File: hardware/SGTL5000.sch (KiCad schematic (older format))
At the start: 23 parts, among them J2 AudioJack3_Ground, J3 AudioJack3_Ground, U6 AP7313-1.8V, U7 SGTL5000

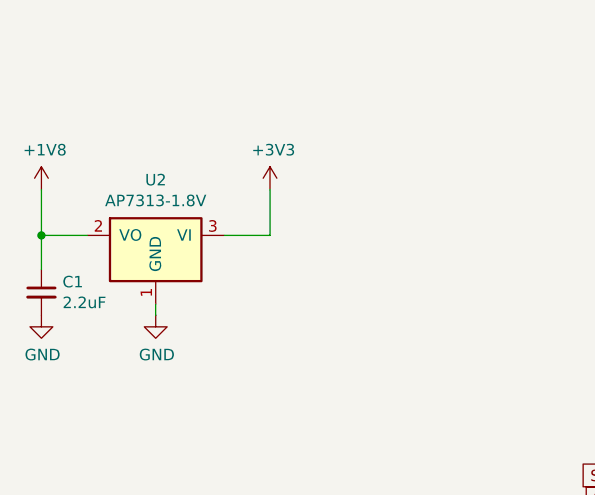
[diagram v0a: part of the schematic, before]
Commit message: notes, check current, add extra decoupling cap for reg, move led supply to 5v
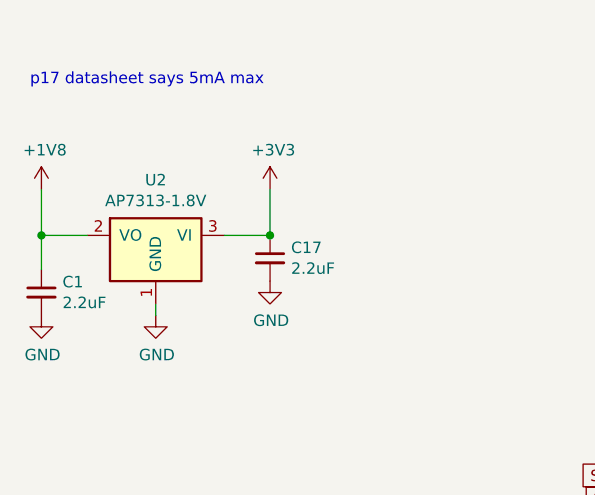
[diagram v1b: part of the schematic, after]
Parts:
- added C17: 2.2uF, Capacitor_SMD:C_0805_2012Metric, symbol Device:C_Small
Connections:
- net +3V3: now also C17.1
- net GND: now also C17.2
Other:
- note added: "p17 datasheet says 5mA max"
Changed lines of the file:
@@
 F 1 "AP7313-1.8V" H 2250 2251 50  0000 C CNN
 F 2 "Package_TO_SOT_SMD:SOT-23" H 2250 2100 50  0001 C CNN
-F 3 "" H 2250 2100 50  0001 C CNN
+F 3 "https://www.diodes.com/assets/Datasheets/AP7313.pdf" H 2250 2100 50  0001 C CNN
 	1    2250 2100
 	1    0    0    -1
@@
 Wire Wire Line
 	4350 3850 4950 3850
+Text Notes 1700 1450 0    50   ~ 0
+p17 datasheet says 5mA max
+$Comp
+L Device:C_Small C?
+U 1 1 5E1A3824
+P 2750 2200
+AR Path="/5E1A3824" Ref="C?"  Part="1"
+AR Path="/5BAC34FB/5E1A3824" Ref="C?"  Part="1"
+AR Path="/5E0E3867/5E1A3824" Ref="C17"  Part="1"
+F 0 "C17" H 2842 2246 50  0000 L CNN
+F 1 "2.2uF" H 2842 2155 50  0000 L CNN
+F 2 "Capacitor_SMD:C_0805_2012Metric" H 2750 2200 50  0001 C CNN
+F 3 "~" H 2750 2200 50  0001 C CNN
+	1    2750 2200
+	1    0    0    -1
+$EndComp
+Connection ~ 2750 2100
+$Comp
+L power:GND #PWR?
+U 1 1 5E1A3C62
+P 2750 2300
+AR Path="/5E1A3C62" Ref="#PWR?"  Part="1"
+AR Path="/5BAC34FB/5E1A3C62" Ref="#PWR?"  Part="1"
+AR Path="/5E0E3867/5E1A3C62" Ref="#PWR03"  Part="1"
+F 0 "#PWR03" H 2750 2050 50  0001 C CNN
+F 1 "GND" H 2755 2127 50  0000 C CNN
+F 2 "" H 2750 2300 50  0001 C CNN
+F 3 "" H 2750 2300 50  0001 C CNN
+	1    2750 2300
+	1    0    0    -1
+$EndComp
 $EndSCHEMATC

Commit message: footprints
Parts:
- C14, C15, C8, C9: value 2.2uF -> 1uF; footprint Capacitor_SMD:C_0805_2012Metric -> Capacitor_SMD:C_1210_3225Metric; farnell (none) -> 2112915
- J2, J3: footprint Connector_Audio:Jack_3.5mm_CUI_SJ-3523-SMT_Horizontal -> audio-fx:Jack_3.5mm_CUI_SJ-3523-SMT_Horizontal; farnell (none) -> 2915138
- U7: farnell (none) -> 2308049
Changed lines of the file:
@@
 F 0 "J1" H 7600 3000 50  0000 R CNN
 F 1 "AudioJack3_Ground" H 7500 3100 50  0001 R CNN
-F 2 "Connector_Audio:Jack_3.5mm_CUI_SJ-3523-SMT_Horizontal" H 7900 3050 50  0001 C CNN
+F 2 "audio-fx:Jack_3.5mm_CUI_SJ-3523-SMT_Horizontal" H 7900 3050 50  0001 C CNN
 F 3 "https://uk.farnell.com/switchcraft-conxall/35rasmt2bhntrx/connector-smt-3-5mm-ph-jk-tap/dp/2915138" H 7900 3050 50  0001 C CNN
+F 4 "2915138" H 7900 3050 50  0001 C CNN "farnell"
 	1    7900 3050
 	-1   0    0    1
@@
 F 0 "J2" H 7600 4150 50  0000 R CNN
 F 1 "AudioJack3_Ground" H 7550 4050 50  0001 R CNN
-F 2 "Connector_Audio:Jack_3.5mm_CUI_SJ-3523-SMT_Horizontal" H 7900 4200 50  0001 C CNN
+F 2 "audio-fx:Jack_3.5mm_CUI_SJ-3523-SMT_Horizontal" H 7900 4200 50  0001 C CNN
 F 3 "~" H 7900 4200 50  0001 C CNN
+F 4 "2915138" H 7900 4200 50  0001 C CNN "farnell"
 	1    7900 4200
 	-1   0    0    1
@@
 AR Path="/5BAC34FB/5BAC3E38" Ref="U7"  Part="1"
 AR Path="/5E0E3867/5BAC3E38" Ref="U3"  Part="1"
-F 0 "U3" H 5650 5000 60  0000 C CNN
-F 1 "SGTL5000" H 5650 4894 60  0000 C CNN
+F 0 "U3" H 5650 3750 60  0000 C CNN
+F 1 "SGTL5000" H 5600 2200 60  0000 C CNN
 F 2 "Package_DFN_QFN:QFN-32-1EP_5x5mm_P0.5mm_EP3.6x3.6mm" H 5650 3800 60  0001 C CNN
 F 3 "https://www.nxp.com/docs/en/data-sheet/SGTL5000.pdf" H 5600 2100 60  0000 C CNN
+F 4 "2308049" H 5650 3750 50  0001 C CNN "farnell"
 	1    5650 3750
 	1    0    0    -1
@@
 AR Path="/5E0E3867/5E146D40" Ref="C8"  Part="1"
 F 0 "C8" V 7042 2996 50  0000 L CNN
-F 1 "2.2uF" V 7150 2900 50  0000 L CNN
-F 2 "Capacitor_SMD:C_0805_2012Metric" H 6950 2950 50  0001 C CNN
-F 3 "~" H 6950 2950 50  0001 C CNN
+F 1 "1uF" V 7150 2900 50  0000 L CNN
+F 2 "Capacitor_SMD:C_1210_3225Metric" H 6950 2950 50  0001 C CNN
+F 3 "http://www.farnell.com/datasheets/199119.pdf" H 6950 2950 50  0001 C CNN
+F 4 "2112915" V 6950 2950 50  0001 C CNN "farnell"
 	1    6950 2950
 	0    -1   -1   0
@@
 AR Path="/5E0E3867/5E147768" Ref="C9"  Part="1"
 F 0 "C9" V 7050 3300 50  0000 L CNN
-F 1 "2.2uF" V 7150 3200 50  0000 L CNN
-F 2 "Capacitor_SMD:C_0805_2012Metric" H 6950 3250 50  0001 C CNN
+F 1 "1uF" V 7150 3200 50  0000 L CNN
+F 2 "Capacitor_SMD:C_1210_3225Metric" H 6950 3250 50  0001 C CNN
 F 3 "~" H 6950 3250 50  0001 C CNN
+F 4 "2112915" H 6950 3250 50  0001 C CNN "farnell"
 	1    6950 3250
 	0    -1   -1   0
@@
 F 0 "J3" H 7600 3750 50  0000 R CNN
 F 1 "AudioJack3_Ground" H 7550 3650 50  0001 R CNN
-F 2 "Connector_Audio:Jack_3.5mm_CUI_SJ-3523-SMT_Horizontal" H 7900 3800 50  0001 C CNN
+F 2 "audio-fx:Jack_3.5mm_CUI_SJ-3523-SMT_Horizontal" H 7900 3800 50  0001 C CNN
 F 3 "~" H 7900 3800 50  0001 C CNN
+F 4 "2915138" H 7900 3800 50  0001 C CNN "farnell"
 	1    7900 3800
 	-1   0    0    1
@@
 AR Path="/5E0E3867/5E1434E0" Ref="C14"  Part="1"
 F 0 "C14" V 7050 3350 50  0000 L CNN
-F 1 "2.2uF" V 7150 3300 50  0000 L CNN
-F 2 "Capacitor_SMD:C_0805_2012Metric" H 6950 3550 50  0001 C CNN
+F 1 "1uF" V 7150 3300 50  0000 L CNN
+F 2 "Capacitor_SMD:C_1210_3225Metric" H 6950 3550 50  0001 C CNN
 F 3 "~" H 6950 3550 50  0001 C CNN
+F 4 "2112915" H 6950 3550 50  0001 C CNN "farnell"
 	1    6950 3550
 	0    -1   -1   0
@@
 AR Path="/5E0E3867/5E143FCC" Ref="C15"  Part="1"
 F 0 "C15" V 6650 3750 50  0000 L CNN
-F 1 "2.2uF" V 6750 3650 50  0000 L CNN
-F 2 "Capacitor_SMD:C_0805_2012Metric" H 6950 3750 50  0001 C CNN
+F 1 "1uF" V 6750 3650 50  0000 L CNN
+F 2 "Capacitor_SMD:C_1210_3225Metric" H 6950 3750 50  0001 C CNN
 F 3 "~" H 6950 3750 50  0001 C CNN
+F 4 "2112915" H 6950 3750 50  0001 C CNN "farnell"
 	1    6950 3750
 	0    -1   -1   0

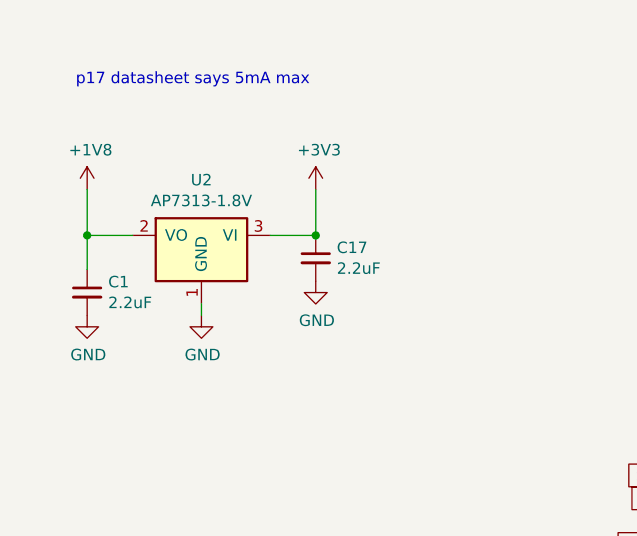
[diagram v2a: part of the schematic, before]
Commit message: changed to LDO that I can source from farnell
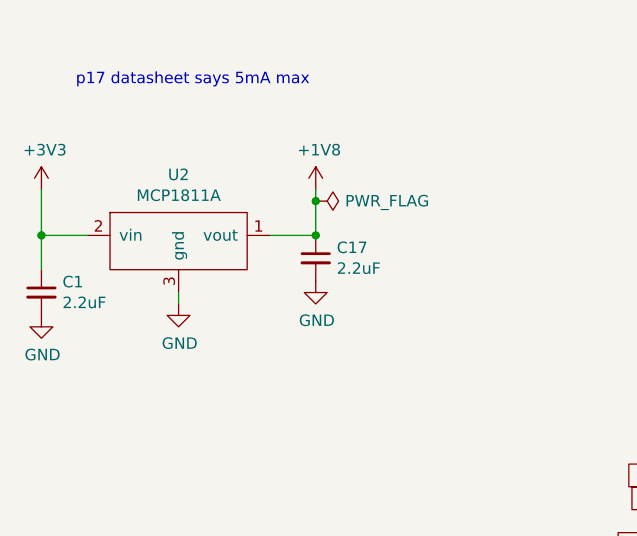
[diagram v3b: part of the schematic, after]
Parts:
- removed U6: AP7313-1.8V, Package_TO_SOT_SMD:SOT-23, symbol teensy-fx-rescue:teensy_beats_parts_AP7313R-1.8V-teensy_beats-cache
- added U2: MCP1811A, Package_TO_SOT_SMD:SOT-23, symbol teensy-fx-rescue:ldo
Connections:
- net +1V8: now also C17.1, U2.1 (vout); no longer C31.1
- net +3V3: now also C31.1, U2.2 (vin); no longer C17.1
- net GND: now also U2.3 (gnd)
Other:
- moved on the sheet: C1
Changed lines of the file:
@@
 	6050 2000 6350 2000
 Connection ~ 6050 2000
-$Comp
-L teensy-fx-rescue:teensy_beats_parts_AP7313R-1.8V-teensy_beats-cache U?
-U 1 1 5BAC54DA
-P 2250 2100
-AR Path="/5BAC54DA" Ref="U?"  Part="1"
-AR Path="/5BAC34FB/5BAC54DA" Ref="U6"  Part="1"
-AR Path="/5E0E3867/5BAC54DA" Ref="U2"  Part="1"
-F 0 "U2" H 2250 2342 50  0000 C CNN
-F 1 "AP7313-1.8V" H 2250 2251 50  0000 C CNN
-F 2 "Package_TO_SOT_SMD:SOT-23" H 2250 2100 50  0001 C CNN
-F 3 "https://www.diodes.com/assets/Datasheets/AP7313.pdf" H 2250 2100 50  0001 C CNN
-	1    2250 2100
-	1    0    0    -1
-$EndComp
-$Comp
-L Device:C_Small C?
-U 1 1 5BAC54E1
-P 1750 2350
-AR Path="/5BAC54E1" Ref="C?"  Part="1"
-AR Path="/5BAC34FB/5BAC54E1" Ref="C31"  Part="1"
-AR Path="/5E0E3867/5BAC54E1" Ref="C1"  Part="1"
-F 0 "C1" H 1842 2396 50  0000 L CNN
-F 1 "2.2uF" H 1842 2305 50  0000 L CNN
-F 2 "Capacitor_SMD:C_0805_2012Metric" H 1750 2350 50  0001 C CNN
-F 3 "~" H 1750 2350 50  0001 C CNN
-	1    1750 2350
-	1    0    0    -1
-$EndComp
-$Comp
-L power:GND #PWR?
-U 1 1 5BAC54E8
-P 1750 2450
-AR Path="/5BAC54E8" Ref="#PWR?"  Part="1"
-AR Path="/5BAC34FB/5BAC54E8" Ref="#PWR0133"  Part="1"
-AR Path="/5E0E3867/5BAC54E8" Ref="#PWR0116"  Part="1"
-F 0 "#PWR0116" H 1750 2200 50  0001 C CNN
-F 1 "GND" H 1755 2277 50  0000 C CNN
-F 2 "" H 1750 2450 50  0001 C CNN
-F 3 "" H 1750 2450 50  0001 C CNN
-	1    1750 2450
-	1    0    0    -1
-$EndComp
-Wire Wire Line
-	1950 2100 1750 2100
-Wire Wire Line
-	1750 2100 1750 2250
-Wire Wire Line
-	2250 2450 2250 2400
+Wire Wire Line
+	2150 2400 2150 2350
 Wire Wire Line
 	2550 2100 2750 2100
 Wire Wire Line
-	2750 2100 2750 1900
-Wire Wire Line
-	1750 2100 1750 1900
-Connection ~ 1750 2100
+	2750 2100 2750 1950
 $Comp
 L power:+3V3 #PWR?
 U 1 1 5BAC54FB
-P 2750 1900
+P 1550 1900
 AR Path="/5BAC54FB" Ref="#PWR?"  Part="1"
 AR Path="/5BAC34FB/5BAC54FB" Ref="#PWR0124"  Part="1"
 AR Path="/5E0E3867/5BAC54FB" Ref="#PWR0118"  Part="1"
-F 0 "#PWR0118" H 2750 1750 50  0001 C CNN
-F 1 "+3V3" H 2765 2073 50  0000 C CNN
-F 2 "" H 2750 1900 50  0001 C CNN
-F 3 "" H 2750 1900 50  0001 C CNN
-	1    2750 1900
-	1    0    0    -1
-$EndComp
-$Comp
-L power:+1V8 #PWR?
-U 1 1 5BAC5501
-P 1750 1900
-AR Path="/5BAC5501" Ref="#PWR?"  Part="1"
-AR Path="/5BAC34FB/5BAC5501" Ref="#PWR0123"  Part="1"
-AR Path="/5E0E3867/5BAC5501" Ref="#PWR0119"  Part="1"
-F 0 "#PWR0119" H 1750 1750 50  0001 C CNN
-F 1 "+1V8" H 1765 2073 50  0000 C CNN
-F 2 "" H 1750 1900 50  0001 C CNN
-F 3 "" H 1750 1900 50  0001 C CNN
-	1    1750 1900
+F 0 "#PWR0118" H 1550 1750 50  0001 C CNN
+F 1 "+3V3" H 1565 2073 50  0000 C CNN
+F 2 "" H 1550 1900 50  0001 C CNN
+F 3 "" H 1550 1900 50  0001 C CNN
+	1    1550 1900
 	1    0    0    -1
 $EndComp
@@
 L power:GND #PWR?
 U 1 1 5BAC54EE
-P 2250 2450
+P 2150 2400
 AR Path="/5BAC54EE" Ref="#PWR?"  Part="1"
 AR Path="/5BAC34FB/5BAC54EE" Ref="#PWR0134"  Part="1"
 AR Path="/5E0E3867/5BAC54EE" Ref="#PWR0117"  Part="1"
-F 0 "#PWR0117" H 2250 2200 50  0001 C CNN
-F 1 "GND" H 2255 2277 50  0000 C CNN
-F 2 "" H 2250 2450 50  0001 C CNN
-F 3 "" H 2250 2450 50  0001 C CNN
-	1    2250 2450
+F 0 "#PWR0117" H 2150 2150 50  0001 C CNN
+F 1 "GND" H 2155 2227 50  0000 C CNN
+F 2 "" H 2150 2400 50  0001 C CNN
+F 3 "" H 2150 2400 50  0001 C CNN
+	1    2150 2400
 	1    0    0    -1
 $EndComp
@@
 	1    0    0    -1
 $EndComp
+$Comp
+L teensy-fx-rescue:ldo U2
+U 1 1 5E1AE9E1
+P 2150 2100
+F 0 "U2" H 2150 2365 50  0000 C CNN
+F 1 "MCP1811A" H 2150 2274 50  0000 C CNN
+F 2 "Package_TO_SOT_SMD:SOT-23" H 2150 2100 50  0001 C CNN
+F 3 "http://www.farnell.com/datasheets/2722379.pdf" H 2150 2100 50  0001 C CNN
+F 4 "2990195" H 2150 2100 50  0001 C CNN "farnell"
+	1    2150 2100
+	1    0    0    -1
+$EndComp
+$Comp
+L power:+1V8 #PWR?
+U 1 1 5BAC5501
+P 2750 1900
+AR Path="/5BAC5501" Ref="#PWR?"  Part="1"
+AR Path="/5BAC34FB/5BAC5501" Ref="#PWR0123"  Part="1"
+AR Path="/5E0E3867/5BAC5501" Ref="#PWR0119"  Part="1"
+F 0 "#PWR0119" H 2750 1750 50  0001 C CNN
+F 1 "+1V8" H 2765 2073 50  0000 C CNN
+F 2 "" H 2750 1900 50  0001 C CNN
+F 3 "" H 2750 1900 50  0001 C CNN
+	1    2750 1900
+	1    0    0    -1
+$EndComp
+Connection ~ 1550 2100
+Wire Wire Line
+	1550 2100 1550 1900
+Wire Wire Line
+	1550 2100 1550 2250
+Wire Wire Line
+	1750 2100 1550 2100
+$Comp
+L power:GND #PWR?
+U 1 1 5BAC54E8
+P 1550 2450
+AR Path="/5BAC54E8" Ref="#PWR?"  Part="1"
+AR Path="/5BAC34FB/5BAC54E8" Ref="#PWR0133"  Part="1"
+AR Path="/5E0E3867/5BAC54E8" Ref="#PWR0116"  Part="1"
+F 0 "#PWR0116" H 1550 2200 50  0001 C CNN
+F 1 "GND" H 1555 2277 50  0000 C CNN
+F 2 "" H 1550 2450 50  0001 C CNN
+F 3 "" H 1550 2450 50  0001 C CNN
+	1    1550 2450
+	1    0    0    -1
+$EndComp
+$Comp
+L Device:C_Small C?
+U 1 1 5BAC54E1
+P 1550 2350
+AR Path="/5BAC54E1" Ref="C?"  Part="1"
+AR Path="/5BAC34FB/5BAC54E1" Ref="C31"  Part="1"
+AR Path="/5E0E3867/5BAC54E1" Ref="C1"  Part="1"
+F 0 "C1" H 1642 2396 50  0000 L CNN
+F 1 "2.2uF" H 1642 2305 50  0000 L CNN
+F 2 "Capacitor_SMD:C_0805_2012Metric" H 1550 2350 50  0001 C CNN
+F 3 "~" H 1550 2350 50  0001 C CNN
+	1    1550 2350
+	1    0    0    -1
+$EndComp
+$Comp
+L power:PWR_FLAG #FLG0104
+U 1 1 5E1CE9B1
+P 2750 1950
+F 0 "#FLG0104" H 2750 2025 50  0001 C CNN
+F 1 "PWR_FLAG" V 2750 2078 50  0000 L CNN
+F 2 "" H 2750 1950 50  0001 C CNN
+F 3 "~" H 2750 1950 50  0001 C CNN
+	1    2750 1950
+	0    1    1    0
+$EndComp
+Connection ~ 2750 1950
+Wire Wire Line
+	2750 1950 2750 1900
 $EndSCHEMATC

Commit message: farnell numbers
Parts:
- C13, C2, C27, C28, C30: farnell (none) -> 1414663
- C17, C26, C29, C31: farnell (none) -> 2773238
- L2: farnell (none) -> 2215655
- R22, R23: farnell (none) -> 1469887
- R3: farnell (none) -> 1469862
- R8, R9: farnell (none) -> 1469860
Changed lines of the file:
@@
 F 2 "Capacitor_SMD:C_0805_2012Metric" H 4550 2250 50  0001 C CNN
 F 3 "~" H 4550 2250 50  0001 C CNN
+F 4 "2773238" H 4550 2250 50  0001 C CNN "farnell"
 	1    4550 2250
 	1    0    0    -1
@@
 F 2 "Capacitor_SMD:C_0805_2012Metric" H 4850 2250 50  0001 C CNN
 F 3 "~" H 4850 2250 50  0001 C CNN
+F 4 "1414663" H 4850 2250 50  0001 C CNN "farnell"
 	1    4850 2250
 	1    0    0    -1
@@
 F 2 "Capacitor_SMD:C_0805_2012Metric" H 5150 2250 50  0001 C CNN
 F 3 "~" H 5150 2250 50  0001 C CNN
+F 4 "1414663" H 5150 2250 50  0001 C CNN "farnell"
 	1    5150 2250
 	1    0    0    -1
@@
 F 2 "Capacitor_SMD:C_0805_2012Metric" H 6350 2250 50  0001 C CNN
 F 3 "~" H 6350 2250 50  0001 C CNN
+F 4 "2773238" H 6350 2250 50  0001 C CNN "farnell"
 	1    6350 2250
 	1    0    0    -1
@@
 F 2 "Capacitor_SMD:C_0805_2012Metric" H 6650 2250 50  0001 C CNN
 F 3 "~" H 6650 2250 50  0001 C CNN
+F 4 "1414663" H 6650 2250 50  0001 C CNN "farnell"
 	1    6650 2250
 	1    0    0    -1
@@
 F 2 "Inductor_SMD:L_0805_2012Metric" V 5780 2000 50  0001 C CNN
 F 3 "~" H 5850 2000 50  0001 C CNN
+F 4 "2215655" H 5850 2000 50  0001 C CNN "farnell"
 	1    5850 2000
 	0    -1   -1   0
@@
 F 2 "Resistor_SMD:R_0805_2012Metric" V 4530 2950 50  0001 C CNN
 F 3 "~" H 4600 2950 50  0001 C CNN
+F 4 "1469887" H 4600 2950 50  0001 C CNN "farnell"
 	1    4600 2950
 	1    0    0    -1
@@
 F 2 "Resistor_SMD:R_0805_2012Metric" V 4830 2950 50  0001 C CNN
 F 3 "~" H 4900 2950 50  0001 C CNN
+F 4 "1469887" H 4900 2950 50  0001 C CNN "farnell"
 	1    4900 2950
 	1    0    0    -1
@@
 F 2 "Capacitor_SMD:C_0805_2012Metric" H 4450 4200 50  0001 C CNN
 F 3 "~" H 4450 4200 50  0001 C CNN
+F 4 "1414663" H 4450 4200 50  0001 C CNN "farnell"
 	1    4450 4200
 	1    0    0    -1
@@
 F 2 "Resistor_SMD:R_0805_2012Metric" V 4430 3450 50  0001 C CNN
 F 3 "~" H 4500 3450 50  0001 C CNN
+F 4 "1469862" H 4500 3450 50  0001 C CNN "farnell"
 	1    4500 3450
 	0    1    1    0
@@
 F 2 "Capacitor_SMD:C_0805_2012Metric" H 6550 4250 50  0001 C CNN
 F 3 "~" H 6550 4250 50  0001 C CNN
+F 4 "1414663" H 6550 4250 50  0001 C CNN "farnell"
 	1    6550 4250
 	1    0    0    -1
@@
 F 2 "Resistor_SMD:R_0805_2012Metric" V 7230 2800 50  0001 C CNN
 F 3 "~" H 7300 2800 50  0001 C CNN
+F 4 "1469860" H 7300 2800 50  0001 C CNN "farnell"
 	1    7300 2800
 	-1   0    0    1
@@
 F 2 "Resistor_SMD:R_0805_2012Metric" V 7430 3200 50  0001 C CNN
 F 3 "~" H 7500 3200 50  0001 C CNN
+F 4 "1469860" H 7500 3200 50  0001 C CNN "farnell"
 	1    7500 3200
 	-1   0    0    1
@@
 F 2 "Capacitor_SMD:C_0805_2012Metric" H 2750 2200 50  0001 C CNN
 F 3 "~" H 2750 2200 50  0001 C CNN
+F 4 "2773238" H 2750 2200 50  0001 C CNN "farnell"
 	1    2750 2200
 	1    0    0    -1
@@
 F 2 "Capacitor_SMD:C_0805_2012Metric" H 1550 2350 50  0001 C CNN
 F 3 "~" H 1550 2350 50  0001 C CNN
+F 4 "2773238" H 1550 2350 50  0001 C CNN "farnell"
 	1    1550 2350
 	1    0    0    -1
